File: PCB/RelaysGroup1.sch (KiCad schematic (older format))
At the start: 25 parts, among them K1 ALQ112, K2 ALQ112, K3 ALQ112, K4 ALQ112, K5 ALQ112, K6 ALQ112, K7 ALQ112, K8 ALQ112, U7 ULN2803A

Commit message: Update PCB.
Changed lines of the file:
@@
 $Descr A4 11693 8268
 encoding utf-8
-Sheet 4 4
-Title ""
-Date ""
-Rev ""
+Sheet 2 4
+Title "Relay board controlled by CAN."
+Date "2021-06-28"
+Rev "1.0"
 Comp ""
 Comment1 ""
@@
 AR Path="/60B86C8D/60AE02BD" Ref="U5"  Part="1"
 AR Path="/60C70E12/60AE02BD" Ref="U6"  Part="1"
-F 0 "U6" H 1750 2167 50  0000 C CNN
+F 0 "U7" H 1750 2167 50  0000 C CNN
 F 1 "ULN2803A" H 1750 2076 50  0000 C CNN
 F 2 "Package_DIP:DIP-18_W7.62mm_LongPads" H 1800 950 50  0001 L CNN
@@
 AR Path="/60B86C8D/60AE02C3" Ref="K10"  Part="1"
 AR Path="/60C70E12/60AE02C3" Ref="K18"  Part="1"
-F 0 "K18" V 5500 1500 50  0000 C CNN
+F 0 "K2" V 5500 1500 50  0000 C CNN
 F 1 "ALQ112" V 5600 1550 50  0000 C CNN
 F 2 "Relay_THT_JGUI:Relay_Panasonic_ALQ112" H 6000 1850 50  0001 L CNN
@@
 AR Path="/60B86C8D/60AE02C9" Ref="K11"  Part="1"
 AR Path="/60C70E12/60AE02C9" Ref="K19"  Part="1"
-F 0 "K19" V 5500 2400 50  0000 C CNN
+F 0 "K3" V 5500 2400 50  0000 C CNN
 F 1 "ALQ112" V 5600 2450 50  0000 C CNN
 F 2 "Relay_THT_JGUI:Relay_Panasonic_ALQ112" H 6000 2750 50  0001 L CNN
@@
 AR Path="/60B86C8D/60AE02CF" Ref="K12"  Part="1"
 AR Path="/60C70E12/60AE02CF" Ref="K20"  Part="1"
-F 0 "K20" V 5500 3300 50  0000 C CNN
+F 0 "K4" V 5500 3300 50  0000 C CNN
 F 1 "ALQ112" V 5600 3350 50  0000 C CNN
 F 2 "Relay_THT_JGUI:Relay_Panasonic_ALQ112" H 6000 3650 50  0001 L CNN
@@
 AR Path="/60B86C8D/60AE079D" Ref="K13"  Part="1"
 AR Path="/60C70E12/60AE079D" Ref="K21"  Part="1"
-F 0 "K21" V 5500 4200 50  0000 C CNN
+F 0 "K5" V 5500 4200 50  0000 C CNN
 F 1 "ALQ112" V 5600 4250 50  0000 C CNN
 F 2 "Relay_THT_JGUI:Relay_Panasonic_ALQ112" H 6000 4550 50  0001 L CNN
@@
 AR Path="/60B86C8D/60AE08E1" Ref="K14"  Part="1"
 AR Path="/60C70E12/60AE08E1" Ref="K22"  Part="1"
-F 0 "K22" V 5500 5100 50  0000 C CNN
+F 0 "K6" V 5500 5100 50  0000 C CNN
 F 1 "ALQ112" V 5600 5150 50  0000 C CNN
 F 2 "Relay_THT_JGUI:Relay_Panasonic_ALQ112" H 6000 5450 50  0001 L CNN
@@
 AR Path="/60B86C8D/60AE08EB" Ref="K15"  Part="1"
 AR Path="/60C70E12/60AE08EB" Ref="K23"  Part="1"
-F 0 "K23" V 5500 6000 50  0000 C CNN
+F 0 "K7" V 5500 6000 50  0000 C CNN
 F 1 "ALQ112" V 5600 6050 50  0000 C CNN
 F 2 "Relay_THT_JGUI:Relay_Panasonic_ALQ112" H 6000 6350 50  0001 L CNN
@@
 AR Path="/60B86C8D/60AE08F5" Ref="K16"  Part="1"
 AR Path="/60C70E12/60AE08F5" Ref="K24"  Part="1"
-F 0 "K24" V 5500 6900 50  0000 C CNN
+F 0 "K8" V 5500 6900 50  0000 C CNN
 F 1 "ALQ112" V 5600 6950 50  0000 C CNN
 F 2 "Relay_THT_JGUI:Relay_Panasonic_ALQ112" H 6000 7250 50  0001 L CNN
@@
 AR Path="/60B86C8D/60AE02B7" Ref="K9"  Part="1"
 AR Path="/60C70E12/60AE02B7" Ref="K17"  Part="1"
-F 0 "K17" V 5500 600 50  0000 C CNN
+F 0 "K1" V 5500 600 50  0000 C CNN
 F 1 "ALQ112" V 5600 650 50  0000 C CNN
 F 2 "Relay_THT_JGUI:Relay_Panasonic_ALQ112" H 6000 950 50  0001 L CNN
@@
 AR Path="/60B86C8D/60E0B3CE" Ref="D9"  Part="1"
 AR Path="/60C70E12/60E0B3CE" Ref="D17"  Part="1"
-F 0 "D17" H 4443 917 50  0000 C CNN
+F 0 "D1" H 4443 917 50  0000 C CNN
 F 1 "LED" H 4443 826 50  0000 C CNN
 F 2 "LED_THT:LED_D3.0mm" H 4450 700 50  0001 C CNN
@@
 AR Path="/60B86C8D/60E0DC26" Ref="R11"  Part="1"
 AR Path="/60C70E12/60E0DC26" Ref="R19"  Part="1"
-F 0 "R19" V 4357 700 50  0000 C CNN
+F 0 "R3" V 4357 700 50  0000 C CNN
 F 1 "1k1" V 4266 700 50  0000 C CNN
 F 2 "Resistor_THT:R_Axial_DIN0207_L6.3mm_D2.5mm_P5.08mm_Vertical" V 4080 700 50  0001 C CNN
@@
 AR Path="/60B86C8D/60E39B0E" Ref="D10"  Part="1"
 AR Path="/60C70E12/60E39B0E" Ref="D18"  Part="1"
-F 0 "D18" H 4443 1817 50  0000 C CNN
+F 0 "D2" H 4443 1817 50  0000 C CNN
 F 1 "LED" H 4443 1726 50  0000 C CNN
 F 2 "LED_THT:LED_D3.0mm" H 4450 1600 50  0001 C CNN
@@
 AR Path="/60B86C8D/60E39D22" Ref="R12"  Part="1"
 AR Path="/60C70E12/60E39D22" Ref="R20"  Part="1"
-F 0 "R20" V 4357 1600 50  0000 C CNN
+F 0 "R4" V 4357 1600 50  0000 C CNN
 F 1 "1k1" V 4266 1600 50  0000 C CNN
 F 2 "Resistor_THT:R_Axial_DIN0207_L6.3mm_D2.5mm_P5.08mm_Vertical" V 4080 1600 50  0001 C CNN
@@
 AR Path="/60B86C8D/60E4C933" Ref="D11"  Part="1"
 AR Path="/60C70E12/60E4C933" Ref="D19"  Part="1"
-F 0 "D19" H 4443 2717 50  0000 C CNN
+F 0 "D3" H 4443 2717 50  0000 C CNN
 F 1 "LED" H 4443 2626 50  0000 C CNN
 F 2 "LED_THT:LED_D3.0mm" H 4450 2500 50  0001 C CNN
@@
 AR Path="/60B86C8D/60E4CB6F" Ref="R13"  Part="1"
 AR Path="/60C70E12/60E4CB6F" Ref="R21"  Part="1"
-F 0 "R21" V 4357 2500 50  0000 C CNN
+F 0 "R5" V 4357 2500 50  0000 C CNN
 F 1 "1k1" V 4266 2500 50  0000 C CNN
 F 2 "Resistor_THT:R_Axial_DIN0207_L6.3mm_D2.5mm_P5.08mm_Vertical" V 4080 2500 50  0001 C CNN
@@
 AR Path="/60B86C8D/60E50D1C" Ref="D12"  Part="1"
 AR Path="/60C70E12/60E50D1C" Ref="D20"  Part="1"
-F 0 "D20" H 4443 3617 50  0000 C CNN
+F 0 "D4" H 4443 3617 50  0000 C CNN
 F 1 "LED" H 4443 3526 50  0000 C CNN
 F 2 "LED_THT:LED_D3.0mm" H 4450 3400 50  0001 C CNN
@@
 AR Path="/60B86C8D/60E50F80" Ref="R14"  Part="1"
 AR Path="/60C70E12/60E50F80" Ref="R22"  Part="1"
-F 0 "R22" V 4357 3400 50  0000 C CNN
+F 0 "R6" V 4357 3400 50  0000 C CNN
 F 1 "1k1" V 4266 3400 50  0000 C CNN
 F 2 "Resistor_THT:R_Axial_DIN0207_L6.3mm_D2.5mm_P5.08mm_Vertical" V 4080 3400 50  0001 C CNN
@@
 AR Path="/60B86C8D/60E550A5" Ref="D13"  Part="1"
 AR Path="/60C70E12/60E550A5" Ref="D21"  Part="1"
-F 0 "D21" H 4443 4517 50  0000 C CNN
+F 0 "D5" H 4443 4517 50  0000 C CNN
 F 1 "LED" H 4443 4426 50  0000 C CNN
 F 2 "LED_THT:LED_D3.0mm" H 4450 4300 50  0001 C CNN
@@
 AR Path="/60B86C8D/60E55331" Ref="R15"  Part="1"
 AR Path="/60C70E12/60E55331" Ref="R23"  Part="1"
-F 0 "R23" V 4357 4300 50  0000 C CNN
+F 0 "R7" V 4357 4300 50  0000 C CNN
 F 1 "1k1" V 4266 4300 50  0000 C CNN
 F 2 "Resistor_THT:R_Axial_DIN0207_L6.3mm_D2.5mm_P5.08mm_Vertical" V 4080 4300 50  0001 C CNN
@@
 AR Path="/60B86C8D/60E591CC" Ref="D14"  Part="1"
 AR Path="/60C70E12/60E591CC" Ref="D22"  Part="1"
-F 0 "D22" H 4443 5417 50  0000 C CNN
+F 0 "D6" H 4443 5417 50  0000 C CNN
 F 1 "LED" H 4443 5326 50  0000 C CNN
 F 2 "LED_THT:LED_D3.0mm" H 4450 5200 50  0001 C CNN
@@
 AR Path="/60B86C8D/60E59480" Ref="R16"  Part="1"
 AR Path="/60C70E12/60E59480" Ref="R24"  Part="1"
-F 0 "R24" V 4357 5200 50  0000 C CNN
+F 0 "R8" V 4357 5200 50  0000 C CNN
 F 1 "1k1" V 4266 5200 50  0000 C CNN
 F 2 "Resistor_THT:R_Axial_DIN0207_L6.3mm_D2.5mm_P5.08mm_Vertical" V 4080 5200 50  0001 C CNN
@@
 AR Path="/60B86C8D/60E5D76B" Ref="D15"  Part="1"
 AR Path="/60C70E12/60E5D76B" Ref="D23"  Part="1"
-F 0 "D23" H 4443 6317 50  0000 C CNN
+F 0 "D7" H 4443 6317 50  0000 C CNN
 F 1 "LED" H 4443 6226 50  0000 C CNN
 F 2 "LED_THT:LED_D3.0mm" H 4450 6100 50  0001 C CNN
@@
 AR Path="/60B86C8D/60E5DA47" Ref="R17"  Part="1"
 AR Path="/60C70E12/60E5DA47" Ref="R25"  Part="1"
-F 0 "R25" V 4357 6100 50  0000 C CNN
+F 0 "R9" V 4357 6100 50  0000 C CNN
 F 1 "1k1" V 4266 6100 50  0000 C CNN
 F 2 "Resistor_THT:R_Axial_DIN0207_L6.3mm_D2.5mm_P5.08mm_Vertical" V 4080 6100 50  0001 C CNN
@@
 AR Path="/60B86C8D/60E62340" Ref="D16"  Part="1"
 AR Path="/60C70E12/60E62340" Ref="D24"  Part="1"
-F 0 "D24" H 4443 7217 50  0000 C CNN
+F 0 "D8" H 4443 7217 50  0000 C CNN
 F 1 "LED" H 4443 7126 50  0000 C CNN
 F 2 "LED_THT:LED_D3.0mm" H 4450 7000 50  0001 C CNN
@@
 AR Path="/60B86C8D/60E62644" Ref="R18"  Part="1"
 AR Path="/60C70E12/60E62644" Ref="R26"  Part="1"
-F 0 "R26" V 4357 7000 50  0000 C CNN
+F 0 "R10" V 4357 7000 50  0000 C CNN
 F 1 "1k1" V 4266 7000 50  0000 C CNN
 F 2 "Resistor_THT:R_Axial_DIN0207_L6.3mm_D2.5mm_P5.08mm_Vertical" V 4080 7000 50  0001 C CNN

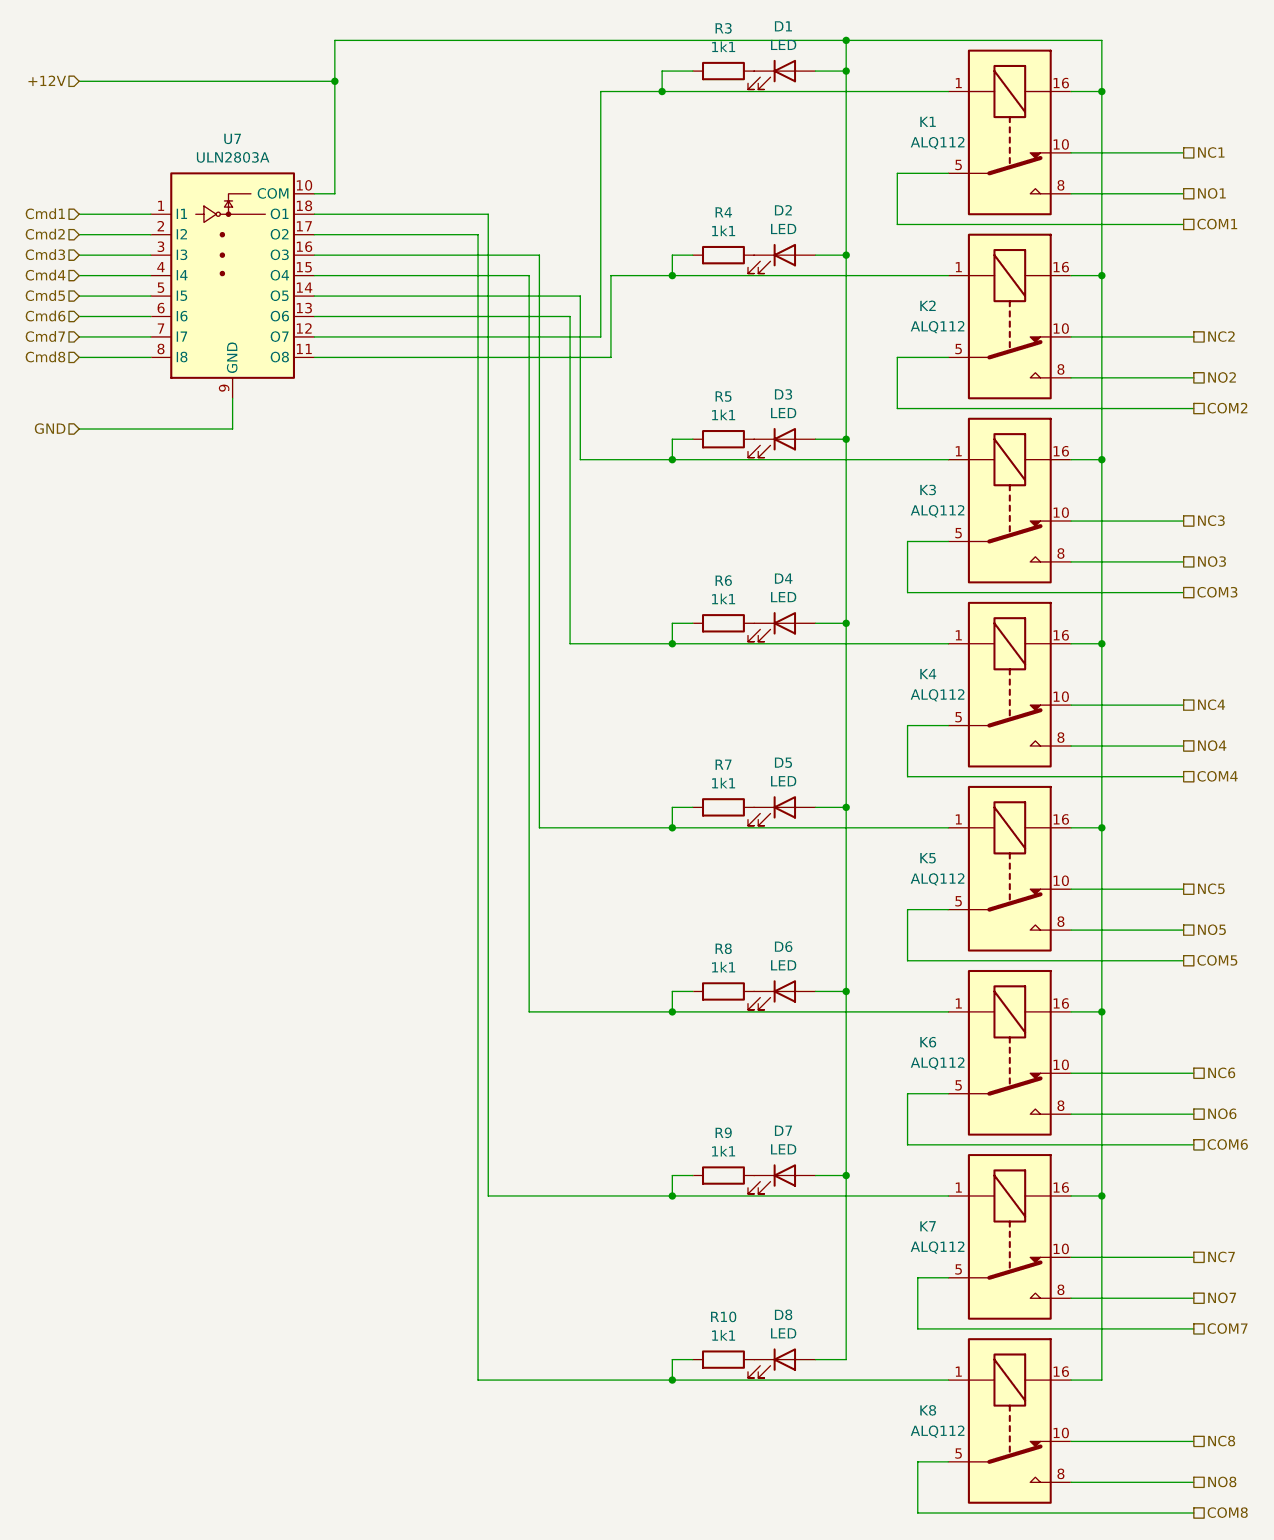
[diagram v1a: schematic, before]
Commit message: Add a jumper to enter configuration mode.
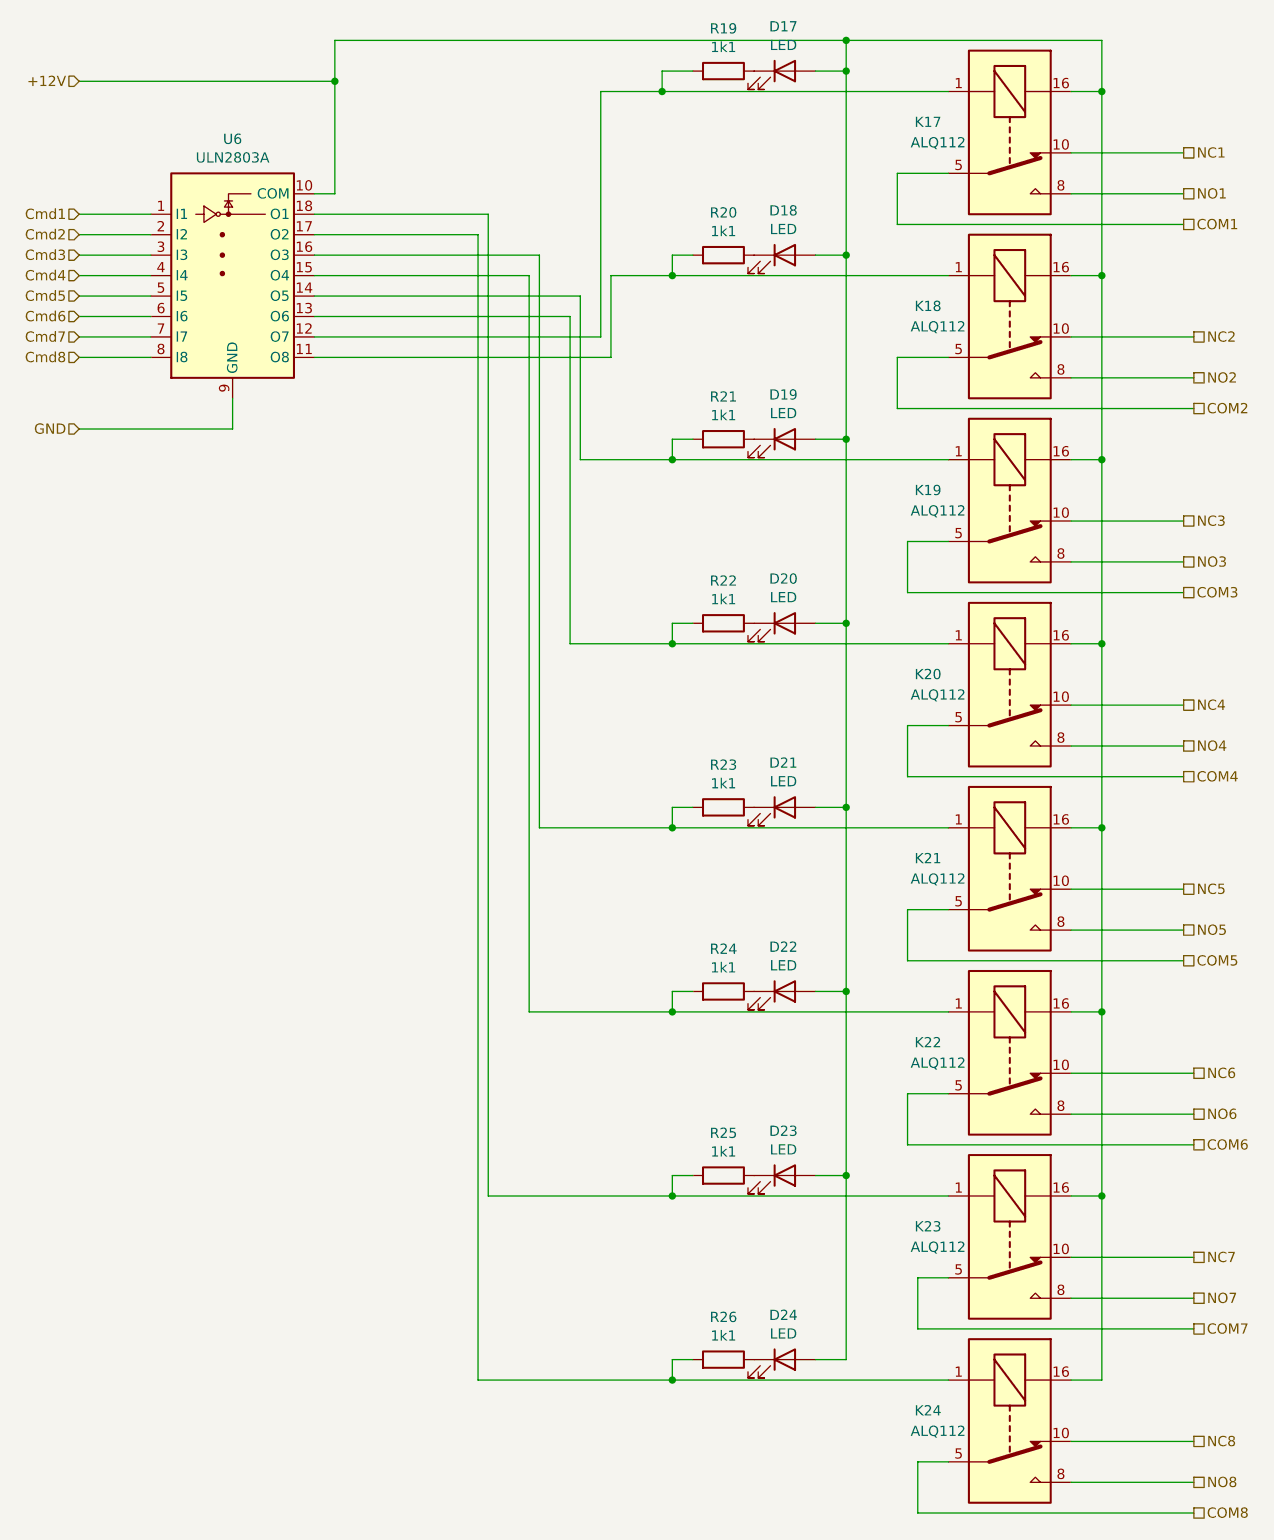
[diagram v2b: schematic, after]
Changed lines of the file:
@@
 AR Path="/60B86C8D/60AE02BD" Ref="U5"  Part="1"
 AR Path="/60C70E12/60AE02BD" Ref="U6"  Part="1"
-F 0 "U7" H 1750 2167 50  0000 C CNN
+F 0 "U6" H 1750 2167 50  0000 C CNN
 F 1 "ULN2803A" H 1750 2076 50  0000 C CNN
 F 2 "Package_DIP:DIP-18_W7.62mm_LongPads" H 1800 950 50  0001 L CNN
@@
 AR Path="/60B86C8D/60AE02C3" Ref="K10"  Part="1"
 AR Path="/60C70E12/60AE02C3" Ref="K18"  Part="1"
-F 0 "K2" V 5500 1500 50  0000 C CNN
+F 0 "K18" V 5500 1500 50  0000 C CNN
 F 1 "ALQ112" V 5600 1550 50  0000 C CNN
 F 2 "Relay_THT_JGUI:Relay_Panasonic_ALQ112" H 6000 1850 50  0001 L CNN
@@
 AR Path="/60B86C8D/60AE02C9" Ref="K11"  Part="1"
 AR Path="/60C70E12/60AE02C9" Ref="K19"  Part="1"
-F 0 "K3" V 5500 2400 50  0000 C CNN
+F 0 "K19" V 5500 2400 50  0000 C CNN
 F 1 "ALQ112" V 5600 2450 50  0000 C CNN
 F 2 "Relay_THT_JGUI:Relay_Panasonic_ALQ112" H 6000 2750 50  0001 L CNN
@@
 AR Path="/60B86C8D/60AE02CF" Ref="K12"  Part="1"
 AR Path="/60C70E12/60AE02CF" Ref="K20"  Part="1"
-F 0 "K4" V 5500 3300 50  0000 C CNN
+F 0 "K20" V 5500 3300 50  0000 C CNN
 F 1 "ALQ112" V 5600 3350 50  0000 C CNN
 F 2 "Relay_THT_JGUI:Relay_Panasonic_ALQ112" H 6000 3650 50  0001 L CNN
@@
 AR Path="/60B86C8D/60AE079D" Ref="K13"  Part="1"
 AR Path="/60C70E12/60AE079D" Ref="K21"  Part="1"
-F 0 "K5" V 5500 4200 50  0000 C CNN
+F 0 "K21" V 5500 4200 50  0000 C CNN
 F 1 "ALQ112" V 5600 4250 50  0000 C CNN
 F 2 "Relay_THT_JGUI:Relay_Panasonic_ALQ112" H 6000 4550 50  0001 L CNN
@@
 AR Path="/60B86C8D/60AE08E1" Ref="K14"  Part="1"
 AR Path="/60C70E12/60AE08E1" Ref="K22"  Part="1"
-F 0 "K6" V 5500 5100 50  0000 C CNN
+F 0 "K22" V 5500 5100 50  0000 C CNN
 F 1 "ALQ112" V 5600 5150 50  0000 C CNN
 F 2 "Relay_THT_JGUI:Relay_Panasonic_ALQ112" H 6000 5450 50  0001 L CNN
@@
 AR Path="/60B86C8D/60AE08EB" Ref="K15"  Part="1"
 AR Path="/60C70E12/60AE08EB" Ref="K23"  Part="1"
-F 0 "K7" V 5500 6000 50  0000 C CNN
+F 0 "K23" V 5500 6000 50  0000 C CNN
 F 1 "ALQ112" V 5600 6050 50  0000 C CNN
 F 2 "Relay_THT_JGUI:Relay_Panasonic_ALQ112" H 6000 6350 50  0001 L CNN
@@
 AR Path="/60B86C8D/60AE08F5" Ref="K16"  Part="1"
 AR Path="/60C70E12/60AE08F5" Ref="K24"  Part="1"
-F 0 "K8" V 5500 6900 50  0000 C CNN
+F 0 "K24" V 5500 6900 50  0000 C CNN
 F 1 "ALQ112" V 5600 6950 50  0000 C CNN
 F 2 "Relay_THT_JGUI:Relay_Panasonic_ALQ112" H 6000 7250 50  0001 L CNN
@@
 AR Path="/60B86C8D/60AE02B7" Ref="K9"  Part="1"
 AR Path="/60C70E12/60AE02B7" Ref="K17"  Part="1"
-F 0 "K1" V 5500 600 50  0000 C CNN
+F 0 "K17" V 5500 600 50  0000 C CNN
 F 1 "ALQ112" V 5600 650 50  0000 C CNN
 F 2 "Relay_THT_JGUI:Relay_Panasonic_ALQ112" H 6000 950 50  0001 L CNN
@@
 AR Path="/60B86C8D/60E0B3CE" Ref="D9"  Part="1"
 AR Path="/60C70E12/60E0B3CE" Ref="D17"  Part="1"
-F 0 "D1" H 4443 917 50  0000 C CNN
+F 0 "D17" H 4443 917 50  0000 C CNN
 F 1 "LED" H 4443 826 50  0000 C CNN
 F 2 "LED_THT:LED_D3.0mm" H 4450 700 50  0001 C CNN
@@
 AR Path="/60B86C8D/60E0DC26" Ref="R11"  Part="1"
 AR Path="/60C70E12/60E0DC26" Ref="R19"  Part="1"
-F 0 "R3" V 4357 700 50  0000 C CNN
+F 0 "R19" V 4357 700 50  0000 C CNN
 F 1 "1k1" V 4266 700 50  0000 C CNN
 F 2 "Resistor_THT:R_Axial_DIN0207_L6.3mm_D2.5mm_P5.08mm_Vertical" V 4080 700 50  0001 C CNN
@@
 AR Path="/60B86C8D/60E39B0E" Ref="D10"  Part="1"
 AR Path="/60C70E12/60E39B0E" Ref="D18"  Part="1"
-F 0 "D2" H 4443 1817 50  0000 C CNN
+F 0 "D18" H 4443 1817 50  0000 C CNN
 F 1 "LED" H 4443 1726 50  0000 C CNN
 F 2 "LED_THT:LED_D3.0mm" H 4450 1600 50  0001 C CNN
@@
 AR Path="/60B86C8D/60E39D22" Ref="R12"  Part="1"
 AR Path="/60C70E12/60E39D22" Ref="R20"  Part="1"
-F 0 "R4" V 4357 1600 50  0000 C CNN
+F 0 "R20" V 4357 1600 50  0000 C CNN
 F 1 "1k1" V 4266 1600 50  0000 C CNN
 F 2 "Resistor_THT:R_Axial_DIN0207_L6.3mm_D2.5mm_P5.08mm_Vertical" V 4080 1600 50  0001 C CNN
@@
 AR Path="/60B86C8D/60E4C933" Ref="D11"  Part="1"
 AR Path="/60C70E12/60E4C933" Ref="D19"  Part="1"
-F 0 "D3" H 4443 2717 50  0000 C CNN
+F 0 "D19" H 4443 2717 50  0000 C CNN
 F 1 "LED" H 4443 2626 50  0000 C CNN
 F 2 "LED_THT:LED_D3.0mm" H 4450 2500 50  0001 C CNN
@@
 AR Path="/60B86C8D/60E4CB6F" Ref="R13"  Part="1"
 AR Path="/60C70E12/60E4CB6F" Ref="R21"  Part="1"
-F 0 "R5" V 4357 2500 50  0000 C CNN
+F 0 "R21" V 4357 2500 50  0000 C CNN
 F 1 "1k1" V 4266 2500 50  0000 C CNN
 F 2 "Resistor_THT:R_Axial_DIN0207_L6.3mm_D2.5mm_P5.08mm_Vertical" V 4080 2500 50  0001 C CNN
@@
 AR Path="/60B86C8D/60E50D1C" Ref="D12"  Part="1"
 AR Path="/60C70E12/60E50D1C" Ref="D20"  Part="1"
-F 0 "D4" H 4443 3617 50  0000 C CNN
+F 0 "D20" H 4443 3617 50  0000 C CNN
 F 1 "LED" H 4443 3526 50  0000 C CNN
 F 2 "LED_THT:LED_D3.0mm" H 4450 3400 50  0001 C CNN
@@
 AR Path="/60B86C8D/60E50F80" Ref="R14"  Part="1"
 AR Path="/60C70E12/60E50F80" Ref="R22"  Part="1"
-F 0 "R6" V 4357 3400 50  0000 C CNN
+F 0 "R22" V 4357 3400 50  0000 C CNN
 F 1 "1k1" V 4266 3400 50  0000 C CNN
 F 2 "Resistor_THT:R_Axial_DIN0207_L6.3mm_D2.5mm_P5.08mm_Vertical" V 4080 3400 50  0001 C CNN
@@
 AR Path="/60B86C8D/60E550A5" Ref="D13"  Part="1"
 AR Path="/60C70E12/60E550A5" Ref="D21"  Part="1"
-F 0 "D5" H 4443 4517 50  0000 C CNN
+F 0 "D21" H 4443 4517 50  0000 C CNN
 F 1 "LED" H 4443 4426 50  0000 C CNN
 F 2 "LED_THT:LED_D3.0mm" H 4450 4300 50  0001 C CNN
@@
 AR Path="/60B86C8D/60E55331" Ref="R15"  Part="1"
 AR Path="/60C70E12/60E55331" Ref="R23"  Part="1"
-F 0 "R7" V 4357 4300 50  0000 C CNN
+F 0 "R23" V 4357 4300 50  0000 C CNN
 F 1 "1k1" V 4266 4300 50  0000 C CNN
 F 2 "Resistor_THT:R_Axial_DIN0207_L6.3mm_D2.5mm_P5.08mm_Vertical" V 4080 4300 50  0001 C CNN
@@
 AR Path="/60B86C8D/60E591CC" Ref="D14"  Part="1"
 AR Path="/60C70E12/60E591CC" Ref="D22"  Part="1"
-F 0 "D6" H 4443 5417 50  0000 C CNN
+F 0 "D22" H 4443 5417 50  0000 C CNN
 F 1 "LED" H 4443 5326 50  0000 C CNN
 F 2 "LED_THT:LED_D3.0mm" H 4450 5200 50  0001 C CNN
@@
 AR Path="/60B86C8D/60E59480" Ref="R16"  Part="1"
 AR Path="/60C70E12/60E59480" Ref="R24"  Part="1"
-F 0 "R8" V 4357 5200 50  0000 C CNN
+F 0 "R24" V 4357 5200 50  0000 C CNN
 F 1 "1k1" V 4266 5200 50  0000 C CNN
 F 2 "Resistor_THT:R_Axial_DIN0207_L6.3mm_D2.5mm_P5.08mm_Vertical" V 4080 5200 50  0001 C CNN
@@
 AR Path="/60B86C8D/60E5D76B" Ref="D15"  Part="1"
 AR Path="/60C70E12/60E5D76B" Ref="D23"  Part="1"
-F 0 "D7" H 4443 6317 50  0000 C CNN
+F 0 "D23" H 4443 6317 50  0000 C CNN
 F 1 "LED" H 4443 6226 50  0000 C CNN
 F 2 "LED_THT:LED_D3.0mm" H 4450 6100 50  0001 C CNN
@@
 AR Path="/60B86C8D/60E5DA47" Ref="R17"  Part="1"
 AR Path="/60C70E12/60E5DA47" Ref="R25"  Part="1"
-F 0 "R9" V 4357 6100 50  0000 C CNN
+F 0 "R25" V 4357 6100 50  0000 C CNN
 F 1 "1k1" V 4266 6100 50  0000 C CNN
 F 2 "Resistor_THT:R_Axial_DIN0207_L6.3mm_D2.5mm_P5.08mm_Vertical" V 4080 6100 50  0001 C CNN
@@
 AR Path="/60B86C8D/60E62340" Ref="D16"  Part="1"
 AR Path="/60C70E12/60E62340" Ref="D24"  Part="1"
-F 0 "D8" H 4443 7217 50  0000 C CNN
+F 0 "D24" H 4443 7217 50  0000 C CNN
 F 1 "LED" H 4443 7126 50  0000 C CNN
 F 2 "LED_THT:LED_D3.0mm" H 4450 7000 50  0001 C CNN
@@
 AR Path="/60B86C8D/60E62644" Ref="R18"  Part="1"
 AR Path="/60C70E12/60E62644" Ref="R26"  Part="1"
-F 0 "R10" V 4357 7000 50  0000 C CNN
+F 0 "R26" V 4357 7000 50  0000 C CNN
 F 1 "1k1" V 4266 7000 50  0000 C CNN
 F 2 "Resistor_THT:R_Axial_DIN0207_L6.3mm_D2.5mm_P5.08mm_Vertical" V 4080 7000 50  0001 C CNN
